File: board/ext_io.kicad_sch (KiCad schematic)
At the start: 34 parts, among them J10 CAN_2, J6 AIN, J7 CAN_1, J8 DIO1, J9 DIO0, U13 25LCxxx, U14 MCP2515-xP, U15 MCP3204, U16 MCP2562-E-P, U17 MCP2515-xP, U18 MCP23S17_SP, U19 MCP2562-E-P, Y2 16MHz, Y3 16MHz

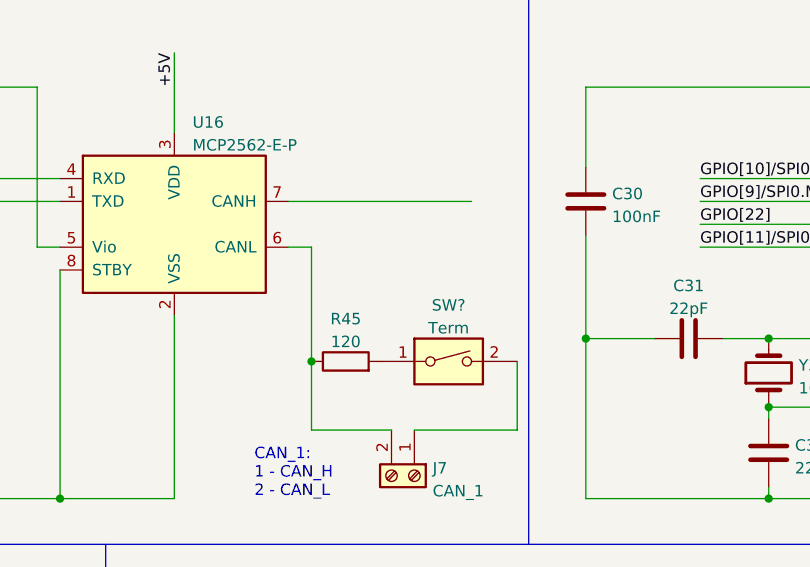
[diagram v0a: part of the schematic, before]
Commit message: Change EEPROM write protection Ppull-up resistor value to 1k.
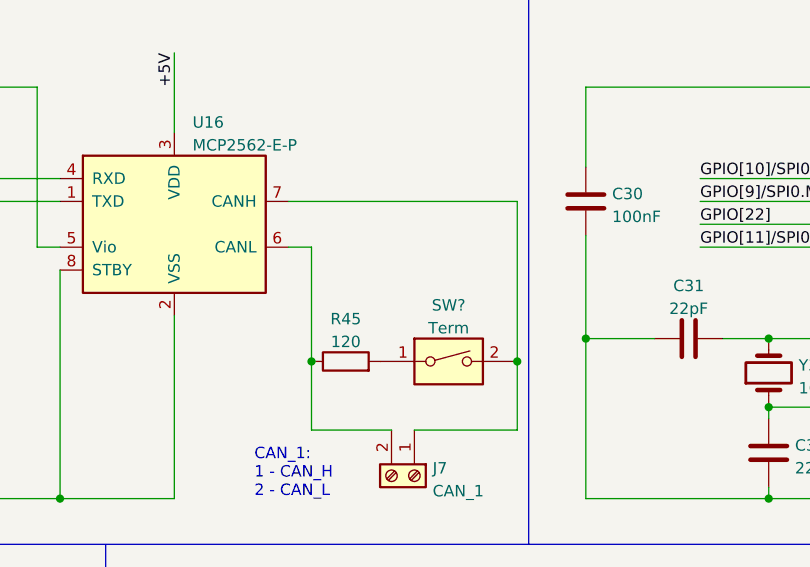
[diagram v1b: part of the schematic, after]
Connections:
- net at J7.1 (Pin_1), SW?.2: now also U16.7 (CANH)
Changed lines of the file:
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@@
   (junction (at 43.18 177.8) (diameter 0) (color 0 0 0 0)
+  )
+  (junction (at 143.51 142.24) (diameter 0) (color 0 0 0 0)
   )
   (junction (at 231.14 30.48) (diameter 0) (color 0 0 0 0)
@@
     (stroke (width 0) (type default) (color 0 0 0 0))
   )
+  (wire (pts (xy 143.51 124.46) (xy 143.51 142.24))
+    (stroke (width 0) (type default) (color 0 0 0 0))
+  )
   (wire (pts (xy 250.19 129.54) (xy 252.73 129.54))
     (stroke (width 0) (type default) (color 0 0 0 0))
@@
     (stroke (width 0) (type default) (color 0 0 0 0))
   )
-  (wire (pts (xy 118.11 124.46) (xy 138.43 124.46))
-    (stroke (width 0) (type default) (color 0 0 0 0))
-  )
+  (wire (pts (xy 118.11 124.46) (xy 143.51 124.46))
+    (stroke (width 0) (type default) (color 0 0 0 0))
+  )

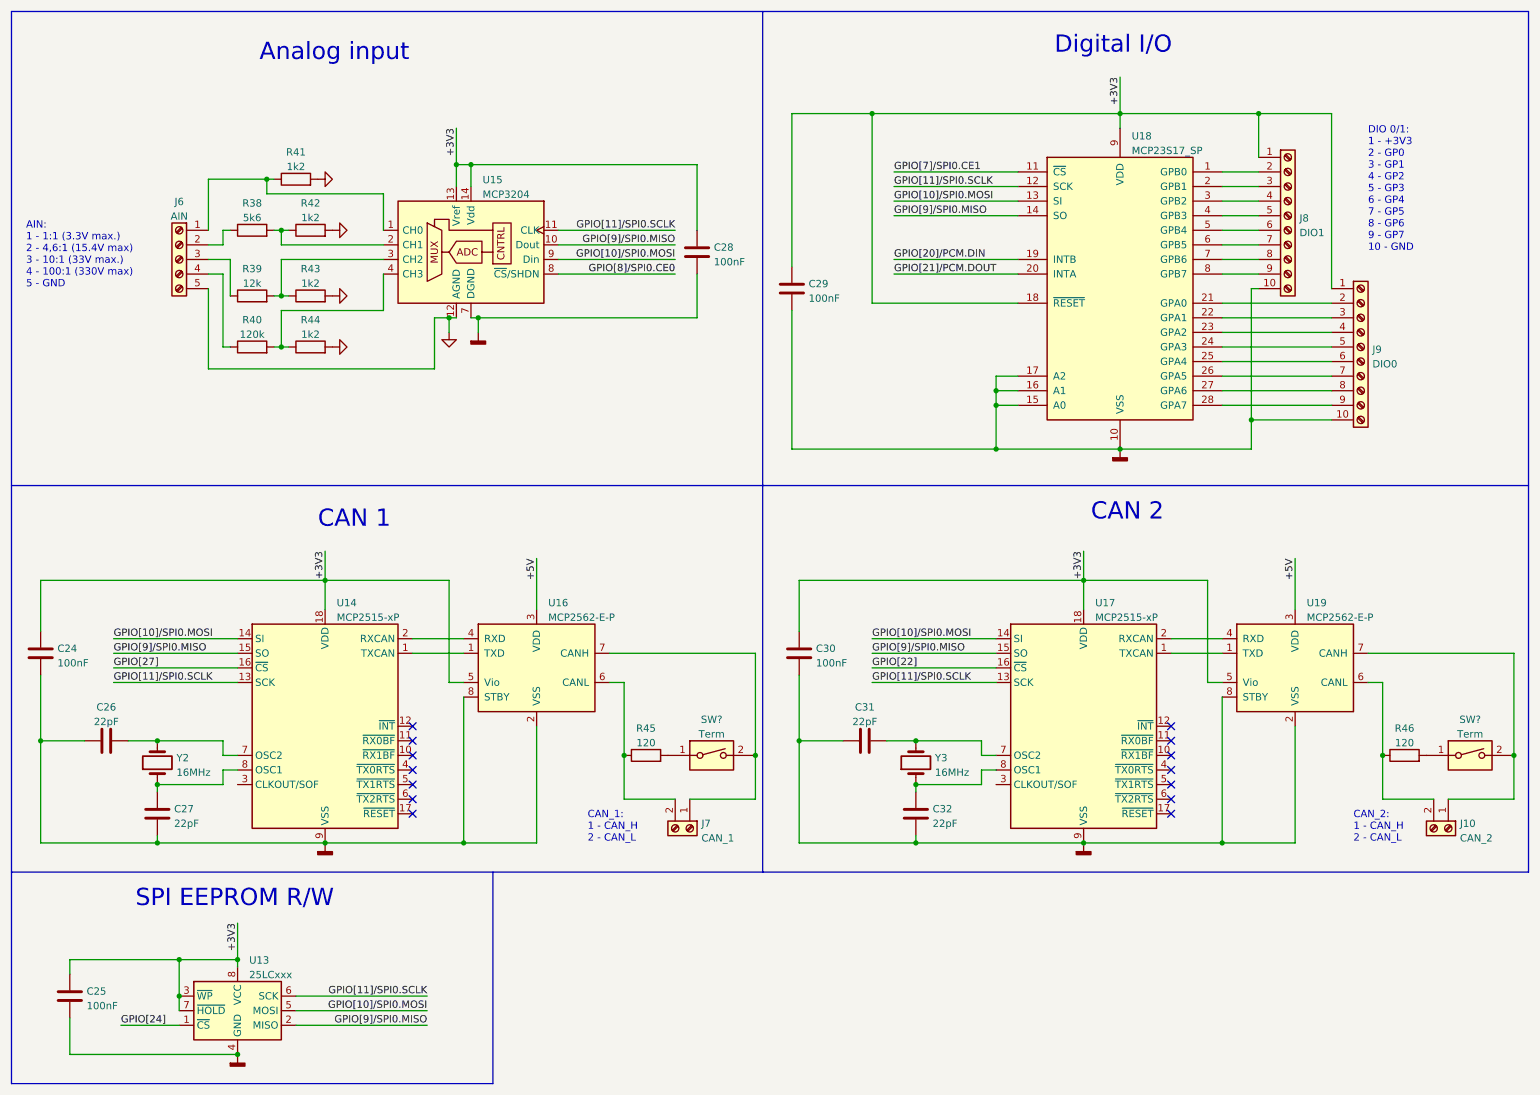
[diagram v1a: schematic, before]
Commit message: Insert polyfuses to protect against short circuit.
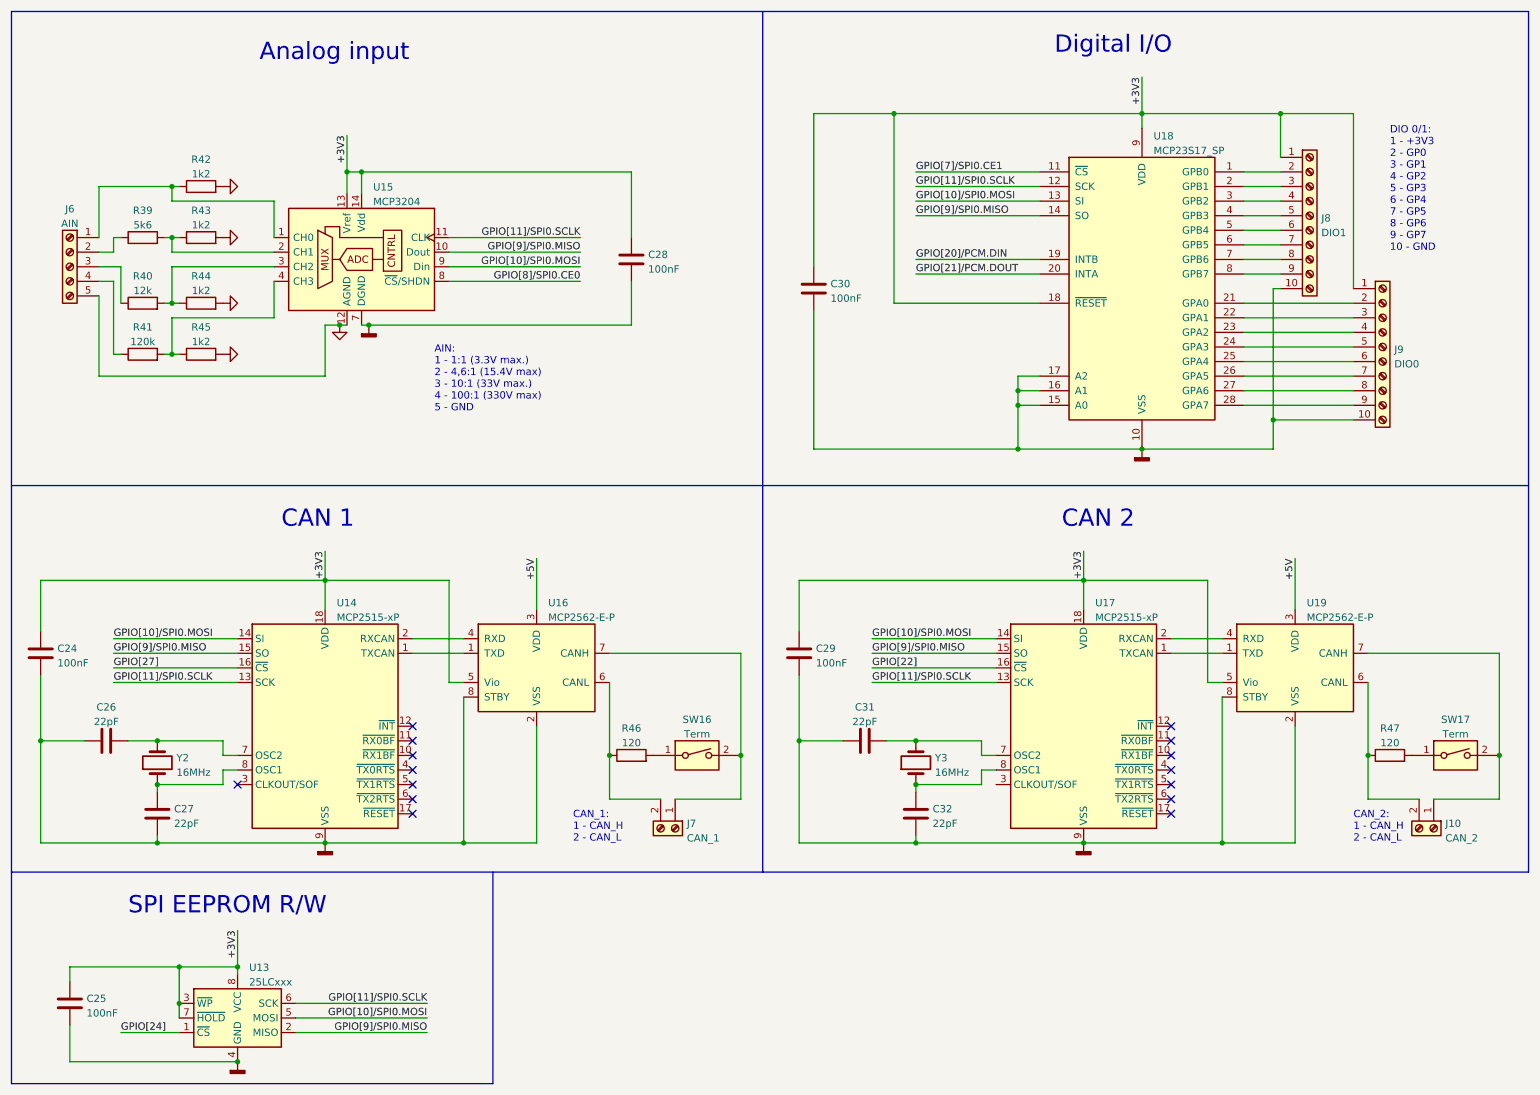
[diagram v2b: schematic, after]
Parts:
- gave numbers to parts that had none: 2
- renumbered C30 to C29, C29 to C30, R38 to R39, R39 to R40, R40 to R41, R41 to R42, R42 to R43, R43 to R44, R44 to R45, R45 to R46, R46 to R47
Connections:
- no-connect marks 14 -> 15
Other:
- moved on the sheet: C25, C28, C30, J10, J6, J7, J8, J9, R39, R40, R41, R42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

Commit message: Improve power circuit and protection.
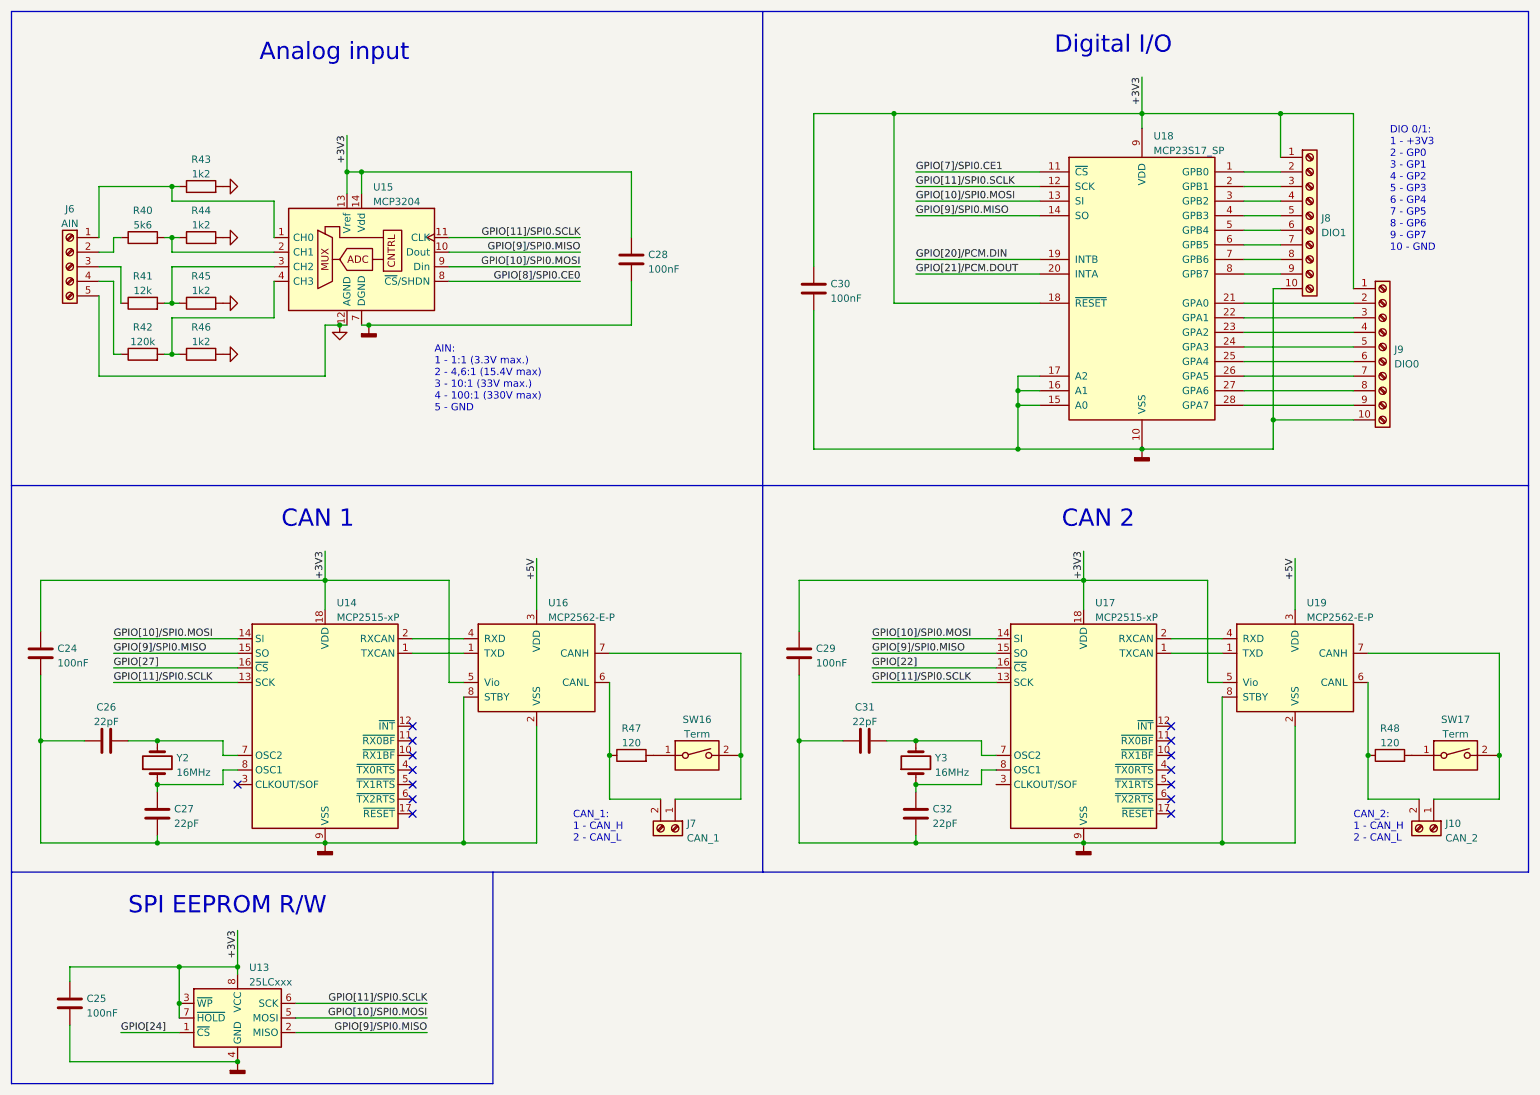
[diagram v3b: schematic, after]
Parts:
- renumbered R39 to R40, R40 to R41, R41 to R42, R42 to R43, R43 to R44, R44 to R45, R45 to R46, R46 to R47, R47 to R48
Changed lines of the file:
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@@
   (symbol (lib_id "Device:R") (at 36.83 72.39 90) (unit 1)
     (in_bom yes) (on_board yes) (fields_autoplaced)
-    (property "Reference" "R41" (id 0) (at 36.83 67.6742 90))
+    (property "Reference" "R42" (id 0) (at 36.83 67.6742 90))
     (property "Value" "120k" (id 1) (at 36.83 70.2111 90))
     (property "Footprint" "" (id 2) (at 36.83 74.168 90)
@@
   (symbol (lib_id "Device:R") (at 254 142.24 90) (unit 1)
     (in_bom yes) (on_board yes) (fields_autoplaced)
-    (property "Reference" "R47" (id 0) (at 254 137.5242 90))
+    (property "Reference" "R48" (id 0) (at 254 137.5242 90))
     (property "Value" "120" (id 1) (at 254 140.0611 90))
     (property "Footprint" "" (id 2) (at 254 144.018 90)
@@
   (symbol (lib_id "Device:R") (at 46.99 72.39 90) (unit 1)
     (in_bom yes) (on_board yes) (fields_autoplaced)
-    (property "Reference" "R45" (id 0) (at 46.99 67.6742 90))
+    (property "Reference" "R46" (id 0) (at 46.99 67.6742 90))
     (property "Value" "1k2" (id 1) (at 46.99 70.2111 90))
     (property "Footprint" "" (id 2) (at 46.99 74.168 90)
@@
   (symbol (lib_id "Device:R") (at 121.92 142.24 90) (unit 1)
     (in_bom yes) (on_board yes) (fields_autoplaced)
-    (property "Reference" "R46" (id 0) (at 121.92 137.5242 90))
+    (property "Reference" "R47" (id 0) (at 121.92 137.5242 90))
     (property "Value" "120" (id 1) (at 121.92 140.0611 90))
     (property "Footprint" "" (id 2) (at 121.92 144.018 90)
@@
   (symbol (lib_id "Device:R") (at 36.83 52.07 90) (unit 1)
     (in_bom yes) (on_board yes) (fields_autoplaced)
-    (property "Reference" "R39" (id 0) (at 36.83 47.3542 90))
+    (property "Reference" "R40" (id 0) (at 36.83 47.3542 90))
     (property "Value" "5k6" (id 1) (at 36.83 49.8911 90))
     (property "Footprint" "" (id 2) (at 36.83 53.848 90)
@@
   (symbol (lib_id "Device:R") (at 46.99 63.5 90) (unit 1)
     (in_bom yes) (on_board yes) (fields_autoplaced)
-    (property "Reference" "R44" (id 0) (at 46.99 58.7842 90))
+    (property "Reference" "R45" (id 0) (at 46.99 58.7842 90))
     (property "Value" "1k2" (id 1) (at 46.99 61.3211 90))
     (property "Footprint" "" (id 2) (at 46.99 65.278 90)
@@
   (symbol (lib_id "Device:R") (at 46.99 43.18 90) (unit 1)
     (in_bom yes) (on_board yes) (fields_autoplaced)
-    (property "Reference" "R42" (id 0) (at 46.99 38.4642 90))
+    (property "Reference" "R43" (id 0) (at 46.99 38.4642 90))
     (property "Value" "1k2" (id 1) (at 46.99 41.0011 90))
     (property "Footprint" "" (id 2) (at 46.99 44.958 90)
@@
   (symbol (lib_id "Device:R") (at 36.83 63.5 90) (unit 1)
     (in_bom yes) (on_board yes) (fields_autoplaced)
-    (property "Reference" "R40" (id 0) (at 36.83 58.7842 90))
+    (property "Reference" "R41" (id 0) (at 36.83 58.7842 90))
     (property "Value" "12k" (id 1) (at 36.83 61.3211 90))
     (property "Footprint" "" (id 2) (at 36.83 65.278 90)
@@
   (symbol (lib_id "Device:R") (at 46.99 52.07 90) (unit 1)
     (in_bom yes) (on_board yes) (fields_autoplaced)
-    (property "Reference" "R43" (id 0) (at 46.99 47.3542 90))
+    (property "Reference" "R44" (id 0) (at 46.99 47.3542 90))
     (property "Value" "1k2" (id 1) (at 46.99 49.8911 90))
     (property "Footprint" "" (id 2) (at 46.99 53.848 90)

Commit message: Do some cleanup after recent changes.
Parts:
- renumbered C24 to C27, C25 to C28, C26 to C29, C27 to C30, C28 to C31, C29 to C32, C30 to C33, C31 to C34, C32 to C35
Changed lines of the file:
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@@
   (title_block
     (title "The Ulysses Board")
-    (date "2022-09-04")
+    (date "2022-09-08")
     (rev "1.3")
     (company "Dirk Gottschalk")
@@
   (symbol (lib_id "Device:C") (at 153.67 60.96 0) (unit 1)
     (in_bom yes) (on_board yes) (fields_autoplaced)
-    (property "Reference" "C30" (id 0) (at 156.591 60.1253 0)
+    (property "Reference" "C33" (id 0) (at 156.591 60.1253 0)
       (effects (font (size 1.27 1.27)) (justify left))
     )
@@
   (symbol (lib_id "Device:C") (at 39.37 152.4 0) (unit 1)
     (in_bom yes) (on_board yes) (fields_autoplaced)
-    (property "Reference" "C27" (id 0) (at 42.291 151.5653 0)
+    (property "Reference" "C30" (id 0) (at 42.291 151.5653 0)
       (effects (font (size 1.27 1.27)) (justify left))
     )
@@
   (symbol (lib_id "Device:C") (at 24.13 185.42 0) (unit 1)
     (in_bom yes) (on_board yes) (fields_autoplaced)
-    (property "Reference" "C25" (id 0) (at 27.051 184.5853 0)
+    (property "Reference" "C28" (id 0) (at 27.051 184.5853 0)
       (effects (font (size 1.27 1.27)) (justify left))
     )
@@
   (symbol (lib_id "Device:C") (at 19.05 124.46 180) (unit 1)
     (in_bom yes) (on_board yes) (fields_autoplaced)
-    (property "Reference" "C24" (id 0) (at 21.971 123.6253 0)
+    (property "Reference" "C27" (id 0) (at 21.971 123.6253 0)
       (effects (font (size 1.27 1.27)) (justify right))
     )
@@
   (symbol (lib_id "Device:C") (at 162.56 139.7 90) (unit 1)
     (in_bom yes) (on_board yes) (fields_autoplaced)
-    (property "Reference" "C31" (id 0) (at 162.56 133.8412 90))
+    (property "Reference" "C34" (id 0) (at 162.56 133.8412 90))
     (property "Value" "22pF" (id 1) (at 162.56 136.3781 90))
     (property "Footprint" "" (id 2) (at 166.37 138.7348 0)
@@
   (symbol (lib_id "Device:C") (at 171.45 152.4 0) (unit 1)
     (in_bom yes) (on_board yes) (fields_autoplaced)
-    (property "Reference" "C32" (id 0) (at 174.371 151.5653 0)
+    (property "Reference" "C35" (id 0) (at 174.371 151.5653 0)
       (effects (font (size 1.27 1.27)) (justify left))
     )
@@
   (symbol (lib_id "Device:C") (at 151.13 124.46 180) (unit 1)
     (in_bom yes) (on_board yes) (fields_autoplaced)
-    (property "Reference" "C29" (id 0) (at 154.051 123.6253 0)
+    (property "Reference" "C32" (id 0) (at 154.051 123.6253 0)
       (effects (font (size 1.27 1.27)) (justify right))
     )
@@
   (symbol (lib_id "Device:C") (at 121.92 55.88 180) (unit 1)
     (in_bom yes) (on_board yes) (fields_autoplaced)
-    (property "Reference" "C28" (id 0) (at 124.841 55.0453 0)
+    (property "Reference" "C31" (id 0) (at 124.841 55.0453 0)
       (effects (font (size 1.27 1.27)) (justify right))
     )
@@
   (symbol (lib_id "Device:C") (at 30.48 139.7 90) (unit 1)
     (in_bom yes) (on_board yes) (fields_autoplaced)
-    (property "Reference" "C26" (id 0) (at 30.48 133.8412 90))
+    (property "Reference" "C29" (id 0) (at 30.48 133.8412 90))
     (property "Value" "22pF" (id 1) (at 30.48 136.3781 90))
     (property "Footprint" "" (id 2) (at 34.29 138.7348 0)
